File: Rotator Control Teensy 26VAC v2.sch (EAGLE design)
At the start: 61 parts, among them K1 G5LE, K2 G5LE, K3 G5LE, Q1 BSS123, Q2 BSS123, Q3 BSS123, U1 MAX7221EWG+T, X1 Rotor, X2 26VAC

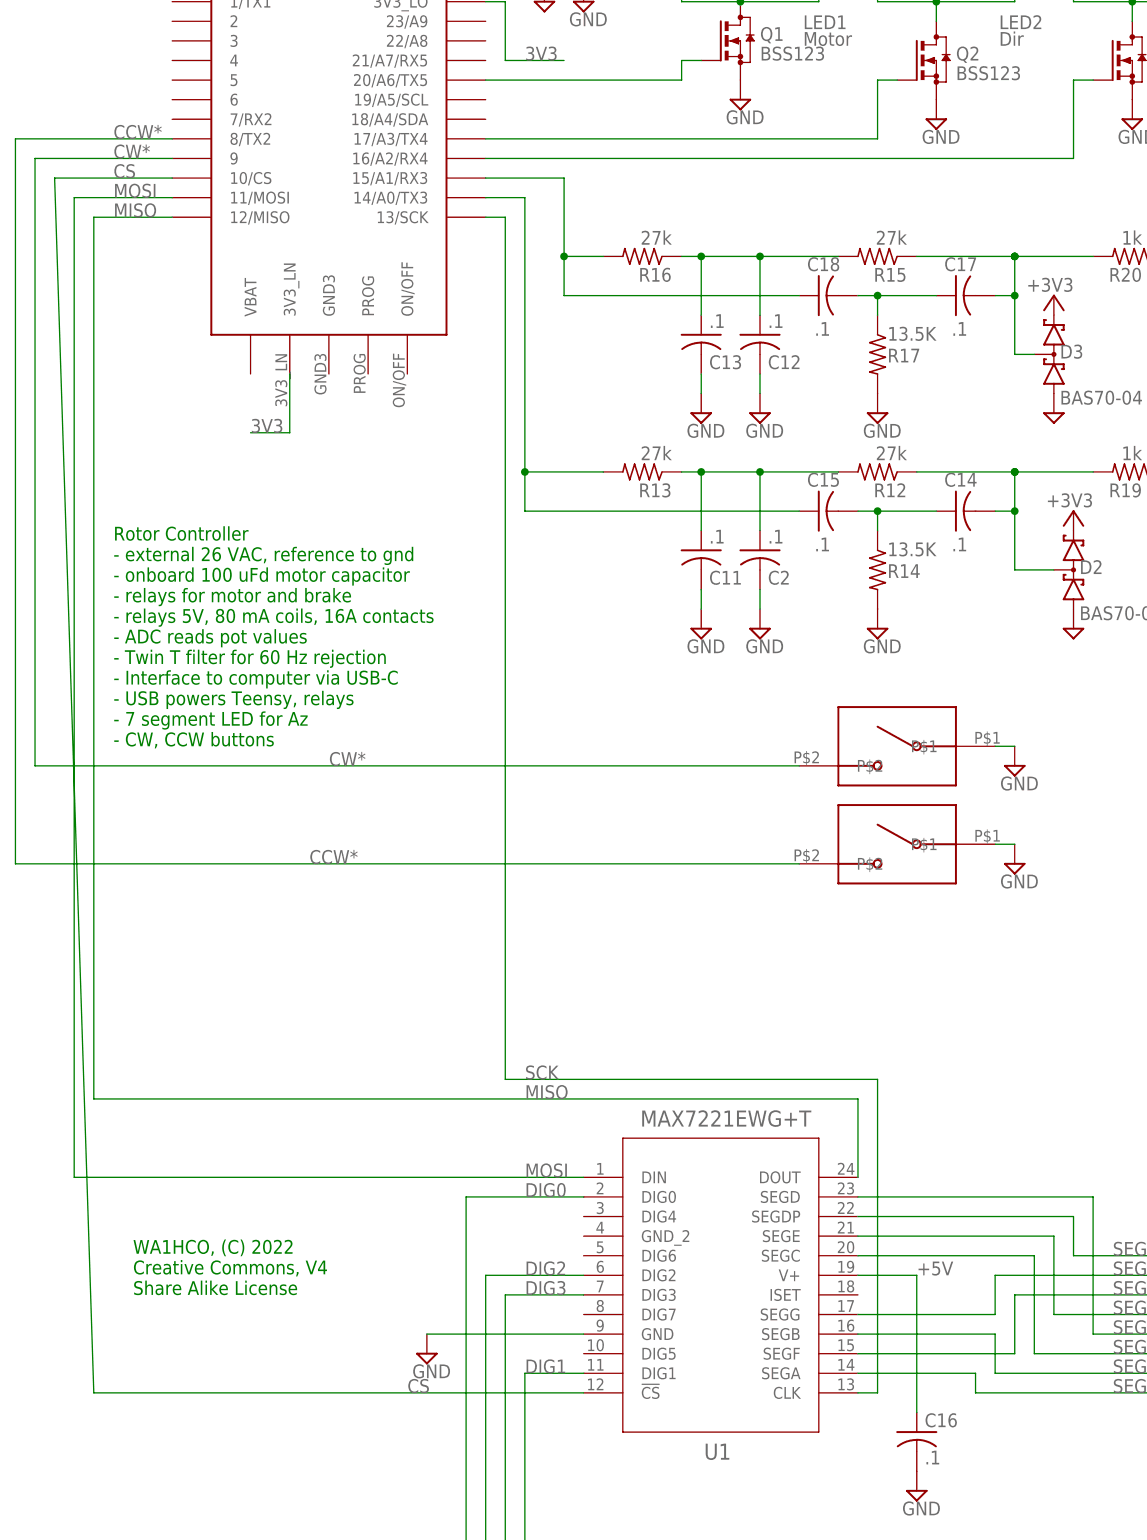
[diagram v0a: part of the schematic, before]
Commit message: Version 2 sent to OSHPark Add pullup on ISET Tweaked a bunch of layout, unecessarily
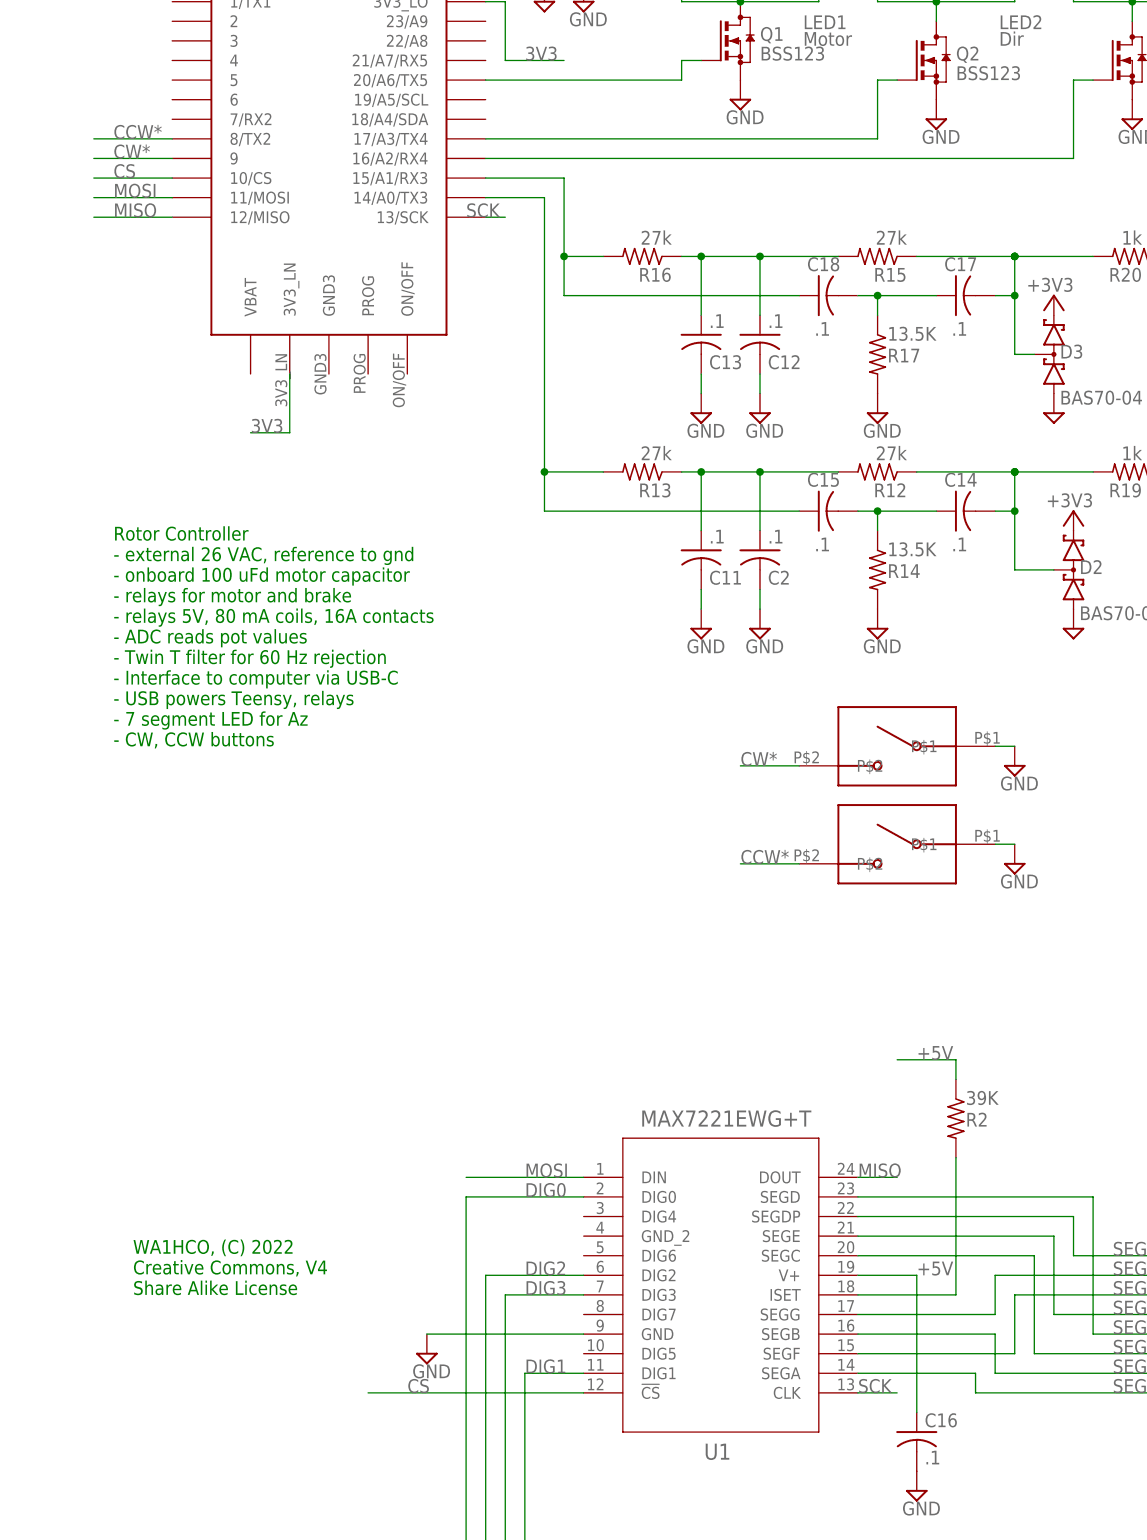
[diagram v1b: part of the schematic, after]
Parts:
- added R2: 39K, rcl:R-US_R0603
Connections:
- new net ISET: R2.2, U1.ISET
- net +5V: now also R2.1
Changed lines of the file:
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@@
 <part name="SUPPLY7" library="supply2" library_urn="urn:adsk.eagle:library:372" deviceset="GND" device=""/>
 <part name="SUPPLY16" library="supply2" library_urn="urn:adsk.eagle:library:372" deviceset="GND" device=""/>
+<part name="R2" library="rcl" library_urn="urn:adsk.eagle:library:334" deviceset="R-US_" device="R0603" package3d_urn="urn:adsk.eagle:package:23555/3" value="39K"/>
 </parts>
 <sheets>
@@
 <attribute name="VALUE" x="145.415" y="-43.815" size="1.778" layer="96"/>
 </instance>
+<instance part="R2" gate="G$1" x="139.7" y="-86.36" smashed="yes" rot="R270">
+<attribute name="NAME" x="140.97" y="-87.4014" size="1.778" layer="95"/>
+<attribute name="VALUE" x="140.97" y="-84.582" size="1.778" layer="96"/>
+</instance>
 </instances>
 <busses>
@@
 <segment>
 <pinref part="U$1" gate="G$1" pin="14/A0/TX3"/>
-<wire x1="83.82" y1="33.02" x2="78.74" y2="33.02" width="0.1524" layer="91"/>
-<wire x1="83.82" y1="-2.54" x2="83.82" y2="33.02" width="0.1524" layer="91"/>
+<wire x1="86.36" y1="33.02" x2="78.74" y2="33.02" width="0.1524" layer="91"/>
+<wire x1="86.36" y1="-2.54" x2="86.36" y2="33.02" width="0.1524" layer="91"/>
 <pinref part="R13" gate="G$1" pin="2"/>
-<wire x1="93.98" y1="-2.54" x2="83.82" y2="-2.54" width="0.1524" layer="91"/>
+<wire x1="93.98" y1="-2.54" x2="86.36" y2="-2.54" width="0.1524" layer="91"/>
 <pinref part="C15" gate="G$1" pin="1"/>
-<wire x1="83.82" y1="-2.54" x2="83.82" y2="-7.62" width="0.1524" layer="91"/>
-<wire x1="83.82" y1="-7.62" x2="119.38" y2="-7.62" width="0.1524" layer="91"/>
-<junction x="83.82" y="-2.54"/>
+<wire x1="86.36" y1="-2.54" x2="86.36" y2="-7.62" width="0.1524" layer="91"/>
+<wire x1="86.36" y1="-7.62" x2="119.38" y2="-7.62" width="0.1524" layer="91"/>
+<junction x="86.36" y="-2.54"/>
 </segment>
 </net>
@@
 <wire x1="127" y1="-106.68" x2="134.62" y2="-106.68" width="0.1524" layer="91"/>
 </segment>
+<segment>
+<pinref part="R2" gate="G$1" pin="1"/>
+<wire x1="139.7" y1="-81.28" x2="139.7" y2="-78.74" width="0.1524" layer="91"/>
+<wire x1="139.7" y1="-78.74" x2="132.08" y2="-78.74" width="0.1524" layer="91"/>
+<label x="134.62" y="-78.74" size="1.778" layer="95"/>
+</segment>
 </net>
 <net name="N$12" class="0">
@@
 <net name="CS" class="0">
 <segment>
+<pinref part="U1" gate="A" pin="!CS"/>
+<wire x1="63.5" y1="-121.92" x2="91.44" y2="-121.92" width="0.1524" layer="91"/>
+<label x="68.58" y="-121.92" size="1.778" layer="95"/>
+</segment>
+<segment>
 <pinref part="U$1" gate="G$1" pin="10/CS"/>
-<wire x1="38.1" y1="35.56" x2="22.86" y2="35.56" width="0.1524" layer="91"/>
-<pinref part="U1" gate="A" pin="!CS"/>
-<wire x1="22.86" y1="35.56" x2="27.94" y2="-121.92" width="0.1524" layer="91"/>
-<wire x1="27.94" y1="-121.92" x2="91.44" y2="-121.92" width="0.1524" layer="91"/>
+<wire x1="38.1" y1="35.56" x2="27.94" y2="35.56" width="0.1524" layer="91"/>
 <label x="30.48" y="35.56" size="1.778" layer="95"/>
-<label x="68.58" y="-121.92" size="1.778" layer="95"/>
 </segment>
 </net>
 <net name="MISO" class="0">
+<segment>
+<pinref part="U1" gate="A" pin="DOUT"/>
+<wire x1="127" y1="-93.98" x2="132.08" y2="-93.98" width="0.1524" layer="91"/>
+<label x="127" y="-93.98" size="1.778" layer="95"/>
+</segment>
 <segment>
 <pinref part="U$1" gate="G$1" pin="12/MISO"/>
 <wire x1="38.1" y1="30.48" x2="27.94" y2="30.48" width="0.1524" layer="91"/>
-<wire x1="27.94" y1="30.48" x2="27.94" y2="-83.82" width="0.1524" layer="91"/>
 <label x="30.48" y="30.48" size="1.778" layer="95"/>
-<pinref part="U1" gate="A" pin="DOUT"/>
-<wire x1="127" y1="-93.98" x2="127" y2="-83.82" width="0.1524" layer="91"/>
-<wire x1="127" y1="-83.82" x2="27.94" y2="-83.82" width="0.1524" layer="91"/>
-<label x="83.82" y="-83.82" size="1.778" layer="95"/>
 </segment>
 </net>
 <net name="SCK" class="0">
+<segment>
+<pinref part="U1" gate="A" pin="CLK"/>
+<wire x1="132.08" y1="-121.92" x2="127" y2="-121.92" width="0.1524" layer="91"/>
+<label x="127" y="-121.92" size="1.778" layer="95"/>
+</segment>
 <segment>
 <pinref part="U$1" gate="G$1" pin="13/SCK"/>
 <wire x1="78.74" y1="30.48" x2="81.28" y2="30.48" width="0.1524" layer="91"/>
-<wire x1="81.28" y1="30.48" x2="81.28" y2="-81.28" width="0.1524" layer="91"/>
-<wire x1="81.28" y1="-81.28" x2="129.54" y2="-81.28" width="0.1524" layer="91"/>
-<pinref part="U1" gate="A" pin="CLK"/>
-<wire x1="129.54" y1="-81.28" x2="129.54" y2="-121.92" width="0.1524" layer="91"/>
-<wire x1="129.54" y1="-121.92" x2="127" y2="-121.92" width="0.1524" layer="91"/>
-<label x="83.82" y="-81.28" size="1.778" layer="95"/>
+<label x="76.2" y="30.48" size="1.778" layer="95"/>
 </segment>
 </net>
 <net name="MOSI" class="0">
 <segment>
+<pinref part="U1" gate="A" pin="DIN"/>
+<wire x1="76.2" y1="-93.98" x2="91.44" y2="-93.98" width="0.1524" layer="91"/>
+<label x="83.82" y="-93.98" size="1.778" layer="95"/>
+</segment>
+<segment>
 <pinref part="U$1" gate="G$1" pin="11/MOSI"/>
-<wire x1="38.1" y1="33.02" x2="25.4" y2="33.02" width="0.1524" layer="91"/>
-<wire x1="25.4" y1="33.02" x2="25.4" y2="-93.98" width="0.1524" layer="91"/>
-<pinref part="U1" gate="A" pin="DIN"/>
-<wire x1="25.4" y1="-93.98" x2="91.44" y2="-93.98" width="0.1524" layer="91"/>
+<wire x1="38.1" y1="33.02" x2="27.94" y2="33.02" width="0.1524" layer="91"/>
 <label x="30.48" y="33.02" size="1.778" layer="95"/>
-<label x="83.82" y="-93.98" size="1.778" layer="95"/>
 </segment>
 </net>
@@
 <segment>
 <pinref part="CCW" gate="G$1" pin="P$2"/>
-<wire x1="17.78" y1="40.64" x2="17.78" y2="-53.34" width="0.1524" layer="91"/>
-<wire x1="17.78" y1="-53.34" x2="119.38" y2="-53.34" width="0.1524" layer="91"/>
+<wire x1="111.76" y1="-53.34" x2="119.38" y2="-53.34" width="0.1524" layer="91"/>
+<label x="111.76" y="-53.34" size="1.778" layer="95"/>
+</segment>
+<segment>
 <pinref part="U$1" gate="G$1" pin="8/TX2"/>
-<wire x1="17.78" y1="40.64" x2="38.1" y2="40.64" width="0.1524" layer="91"/>
-<label x="55.88" y="-53.34" size="1.778" layer="95"/>
+<wire x1="27.94" y1="40.64" x2="38.1" y2="40.64" width="0.1524" layer="91"/>
 <label x="30.48" y="40.64" size="1.778" layer="95"/>
 </segment>
@@
 <segment>
 <pinref part="CW" gate="G$1" pin="P$2"/>
-<wire x1="20.32" y1="38.1" x2="20.32" y2="-40.64" width="0.1524" layer="91"/>
-<wire x1="20.32" y1="-40.64" x2="119.38" y2="-40.64" width="0.1524" layer="91"/>
+<wire x1="111.76" y1="-40.64" x2="119.38" y2="-40.64" width="0.1524" layer="91"/>
+<label x="111.76" y="-40.64" size="1.778" layer="95"/>
+</segment>
+<segment>
 <pinref part="U$1" gate="G$1" pin="9"/>
-<wire x1="38.1" y1="38.1" x2="20.32" y2="38.1" width="0.1524" layer="91"/>
-<label x="58.42" y="-40.64" size="1.778" layer="95"/>
+<wire x1="38.1" y1="38.1" x2="27.94" y2="38.1" width="0.1524" layer="91"/>
 <label x="30.48" y="38.1" size="1.778" layer="95"/>
 </segment>
 </net>
+<net name="ISET" class="0">
+<segment>
+<pinref part="R2" gate="G$1" pin="2"/>
+<wire x1="139.7" y1="-91.44" x2="139.7" y2="-109.22" width="0.1524" layer="91"/>
+<pinref part="U1" gate="A" pin="ISET"/>
+<wire x1="139.7" y1="-109.22" x2="127" y2="-109.22" width="0.1524" layer="91"/>
+</segment>
+</net>

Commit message: Moved overvoltage protect diodes to after the 60 Hz notch filter.  So the 60 Hz doesn't cause clipping and a DC shift when DC is near zero.
Tweaked the layout accordingly.
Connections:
- net N$1: no longer D3.C1A2
- net N$23: now also D3.C1A2
- net N$3: no longer D2.C1A2
- net N$7: now also D2.C1A2
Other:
- moved on the sheet: C11, C12, C13, C14, C15, C17, C18, C2, D2, D3, R12, R13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

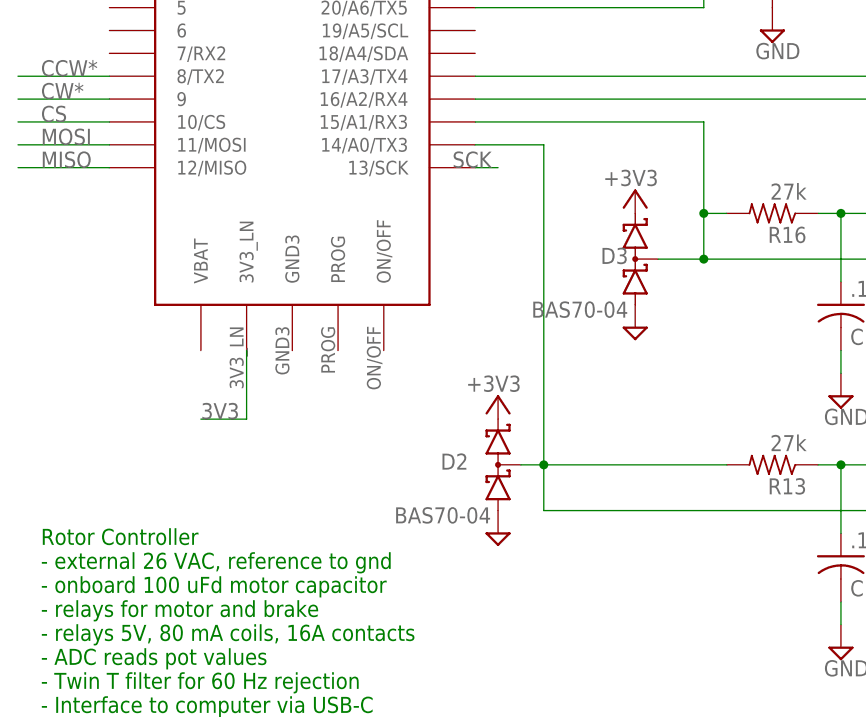
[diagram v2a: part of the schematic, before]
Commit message: Move OVP diodes close to ADC
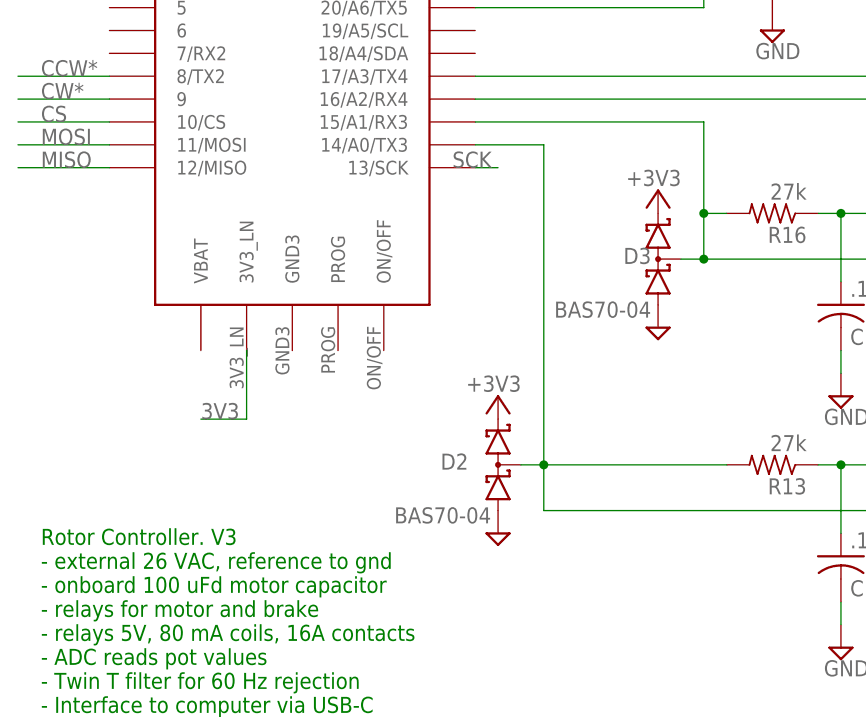
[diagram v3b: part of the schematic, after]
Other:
- note added: "Rotor Controller. V3 - external 26 VAC, reference to gnd - onboard 100 uFd motor capacitor - relays for motor and brake - relays 5V, 80 mA coils, 16A contacts - ADC reads pot values - Twin T filter for 60 Hz rejection - Interface to computer via USB-C - USB powers Teensy, relays - 7 segment LED for Az - CW, CCW buttons"
- note removed: "Rotor Controller - external 26 VAC, reference to gnd - onboard 100 uFd motor capacitor - relays for motor and brake - relays 5V, 80 mA coils, 16A contacts - ADC reads pot values - Twin T filter for 60 Hz rejection - Interface to computer via USB-C - USB powers Teensy, relays - 7 segment LED for Az - CW, CCW buttons"
- moved on the sheet: D3
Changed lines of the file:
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@@
 <sheet>
 <plain>
-<text x="30.48" y="-38.1" size="1.778" layer="91">Rotor Controller
+<text x="30.48" y="-38.1" size="1.778" layer="91">Rotor Controller. V3
 - external 26 VAC, reference to gnd
 - onboard 100 uFd motor capacitor
@@
 <attribute name="VALUE" x="80.518" y="-9.0424" size="1.778" layer="96" rot="MR0"/>
 </instance>
-<instance part="D3" gate="G$1" x="96.52" y="20.32" smashed="yes" rot="MR90">
-<attribute name="NAME" x="95.758" y="19.7866" size="1.778" layer="95" rot="MR0"/>
-<attribute name="VALUE" x="95.758" y="13.8176" size="1.778" layer="96" rot="MR0"/>
+<instance part="D3" gate="G$1" x="99.06" y="20.32" smashed="yes" rot="MR90">
+<attribute name="NAME" x="98.298" y="19.7866" size="1.778" layer="95" rot="MR0"/>
+<attribute name="VALUE" x="98.298" y="13.8176" size="1.778" layer="96" rot="MR0"/>
 </instance>
 <instance part="SUPPLY27" gate="GND" x="81.28" y="-10.16" smashed="yes"/>
-<instance part="SUPPLY28" gate="GND" x="96.52" y="12.7" smashed="yes"/>
+<instance part="SUPPLY28" gate="GND" x="99.06" y="12.7" smashed="yes"/>
 <instance part="+3V3" gate="G$1" x="81.28" y="5.08" smashed="yes">
 <attribute name="VALUE" x="77.724" y="5.588" size="1.778" layer="96"/>
 </instance>
-<instance part="+3V4" gate="G$1" x="96.52" y="27.94" smashed="yes">
-<attribute name="VALUE" x="92.964" y="28.448" size="1.778" layer="96"/>
+<instance part="+3V4" gate="G$1" x="99.06" y="27.94" smashed="yes">
+<attribute name="VALUE" x="95.504" y="28.448" size="1.778" layer="96"/>
 </instance>
 <instance part="C1" gate="G$1" x="195.58" y="116.84" smashed="yes">
@@
 <wire x1="104.14" y1="35.56" x2="78.74" y2="35.56" width="0.1524" layer="91"/>
 <pinref part="D3" gate="G$1" pin="C1A2"/>
-<wire x1="99.06" y1="20.32" x2="104.14" y2="20.32" width="0.1524" layer="91"/>
+<wire x1="101.6" y1="20.32" x2="104.14" y2="20.32" width="0.1524" layer="91"/>
 <wire x1="104.14" y1="20.32" x2="104.14" y2="25.4" width="0.1524" layer="91"/>
 <junction x="104.14" y="20.32"/>
